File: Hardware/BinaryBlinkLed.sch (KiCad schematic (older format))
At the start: 16 parts

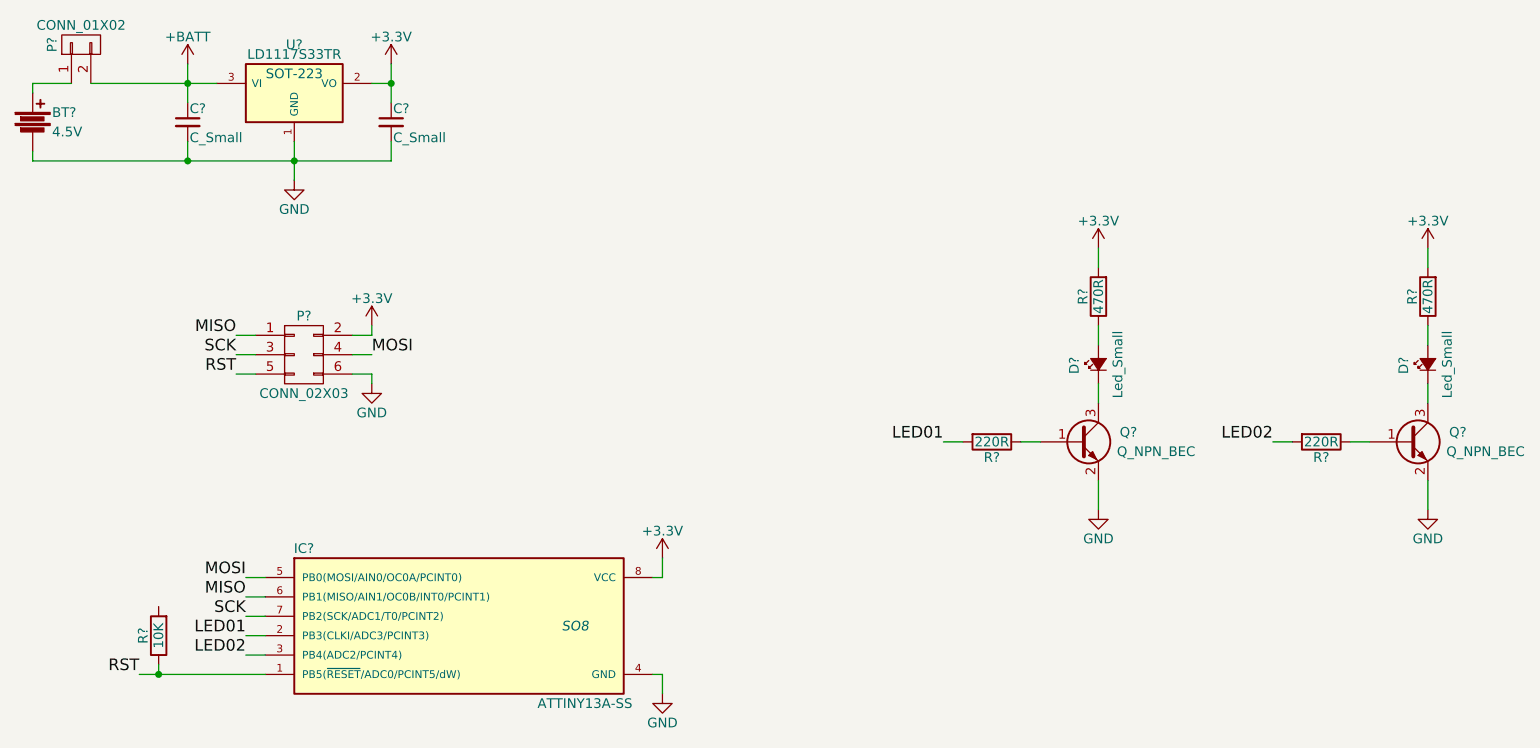
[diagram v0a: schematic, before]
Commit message: set value and name of some components
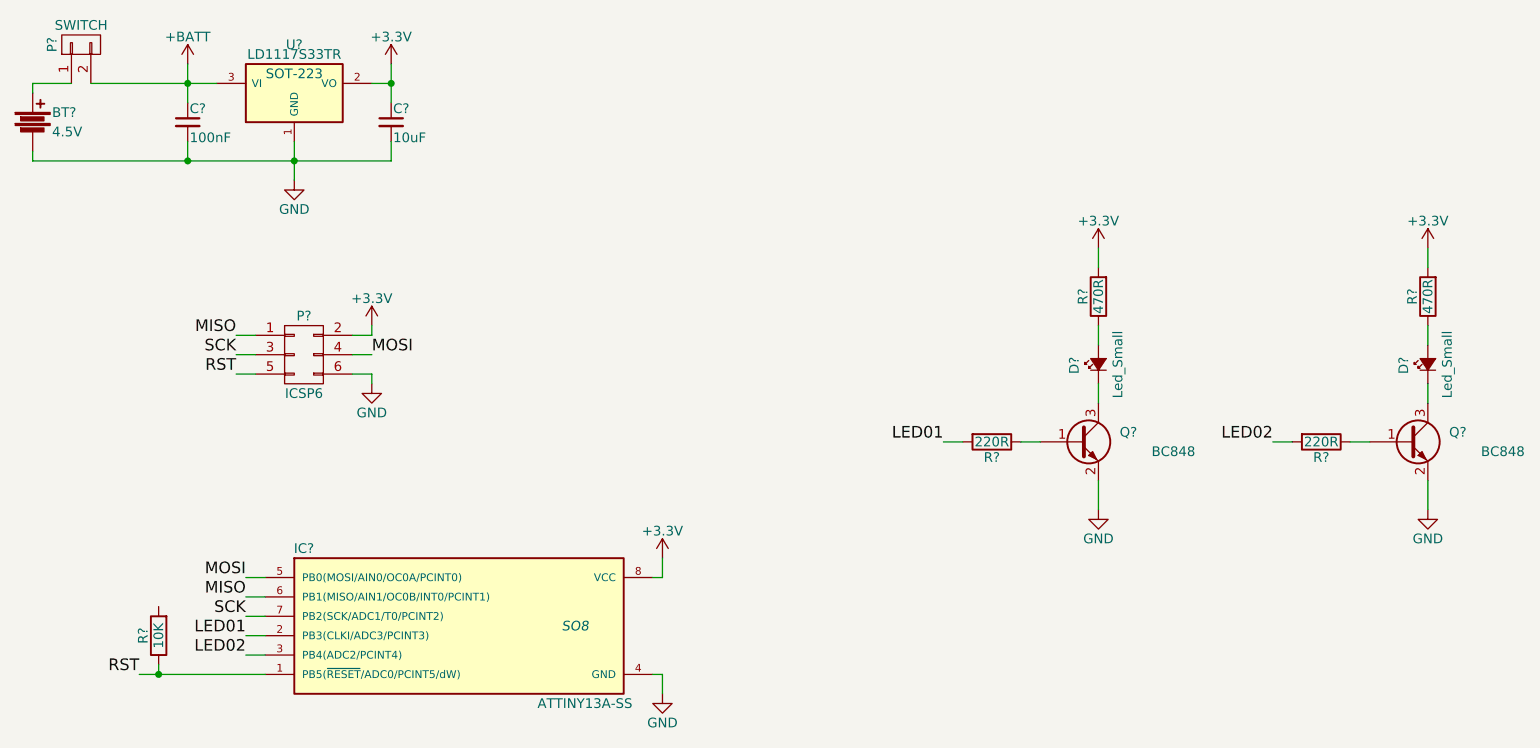
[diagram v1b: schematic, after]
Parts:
- C?: value C_Small -> 100nF
- C?: value C_Small -> 10uF
- P?: value CONN_01X02 -> SWITCH
- P?: value CONN_02X03 -> ICSP6
- Q? (x2): value Q_NPN_BEC -> BC848
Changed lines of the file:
@@
 LIBS:contrib
 LIBS:valves
+LIBS:BinaryBlinkLed-cache
 EELAYER 25 0
 EELAYER END
@@
 P 6800 3550
 F 0 "Q?" H 7100 3600 50  0000 R CNN
-F 1 "Q_NPN_BEC" H 7400 3500 50  0000 R CNN
+F 1 "BC848" H 7400 3500 50  0000 R CNN
 F 2 "" H 7000 3650 50  0000 C CNN
 F 3 "" H 6800 3550 50  0000 C CNN
@@
 P 1650 1500
 F 0 "P?" H 1650 1650 50  0000 C CNN
-F 1 "CONN_01X02" V 1750 1500 50  0000 C CNN
+F 1 "SWITCH" V 1750 1500 50  0000 C CNN
 F 2 "" H 1650 1500 50  0000 C CNN
 F 3 "" H 1650 1500 50  0000 C CNN
@@
 P 8500 3550
 F 0 "Q?" H 8800 3600 50  0000 R CNN
-F 1 "Q_NPN_BEC" H 9100 3500 50  0000 R CNN
+F 1 "BC848" H 9100 3500 50  0000 R CNN
 F 2 "" H 8700 3650 50  0000 C CNN
 F 3 "" H 8500 3550 50  0000 C CNN
@@
 P 2200 1900
 F 0 "C?" H 2210 1970 50  0000 L CNN
-F 1 "C_Small" H 2210 1820 50  0000 L CNN
+F 1 "100nF" H 2210 1820 50  0000 L CNN
 F 2 "" H 2200 1900 50  0000 C CNN
 F 3 "" H 2200 1900 50  0000 C CNN
@@
 P 3250 1900
 F 0 "C?" H 3260 1970 50  0000 L CNN
-F 1 "C_Small" H 3260 1820 50  0000 L CNN
+F 1 "10uF" H 3260 1820 50  0000 L CNN
 F 2 "" H 3250 1900 50  0000 C CNN
 F 3 "" H 3250 1900 50  0000 C CNN
@@
 P 2800 3100
 F 0 "P?" H 2800 3300 50  0000 C CNN
-F 1 "CONN_02X03" H 2800 2900 50  0000 C CNN
+F 1 "ICSP6" H 2800 2900 50  0000 C CNN
 F 2 "" H 2800 1900 50  0000 C CNN
 F 3 "" H 2800 1900 50  0000 C CNN
